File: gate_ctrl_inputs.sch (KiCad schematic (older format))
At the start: 6 parts

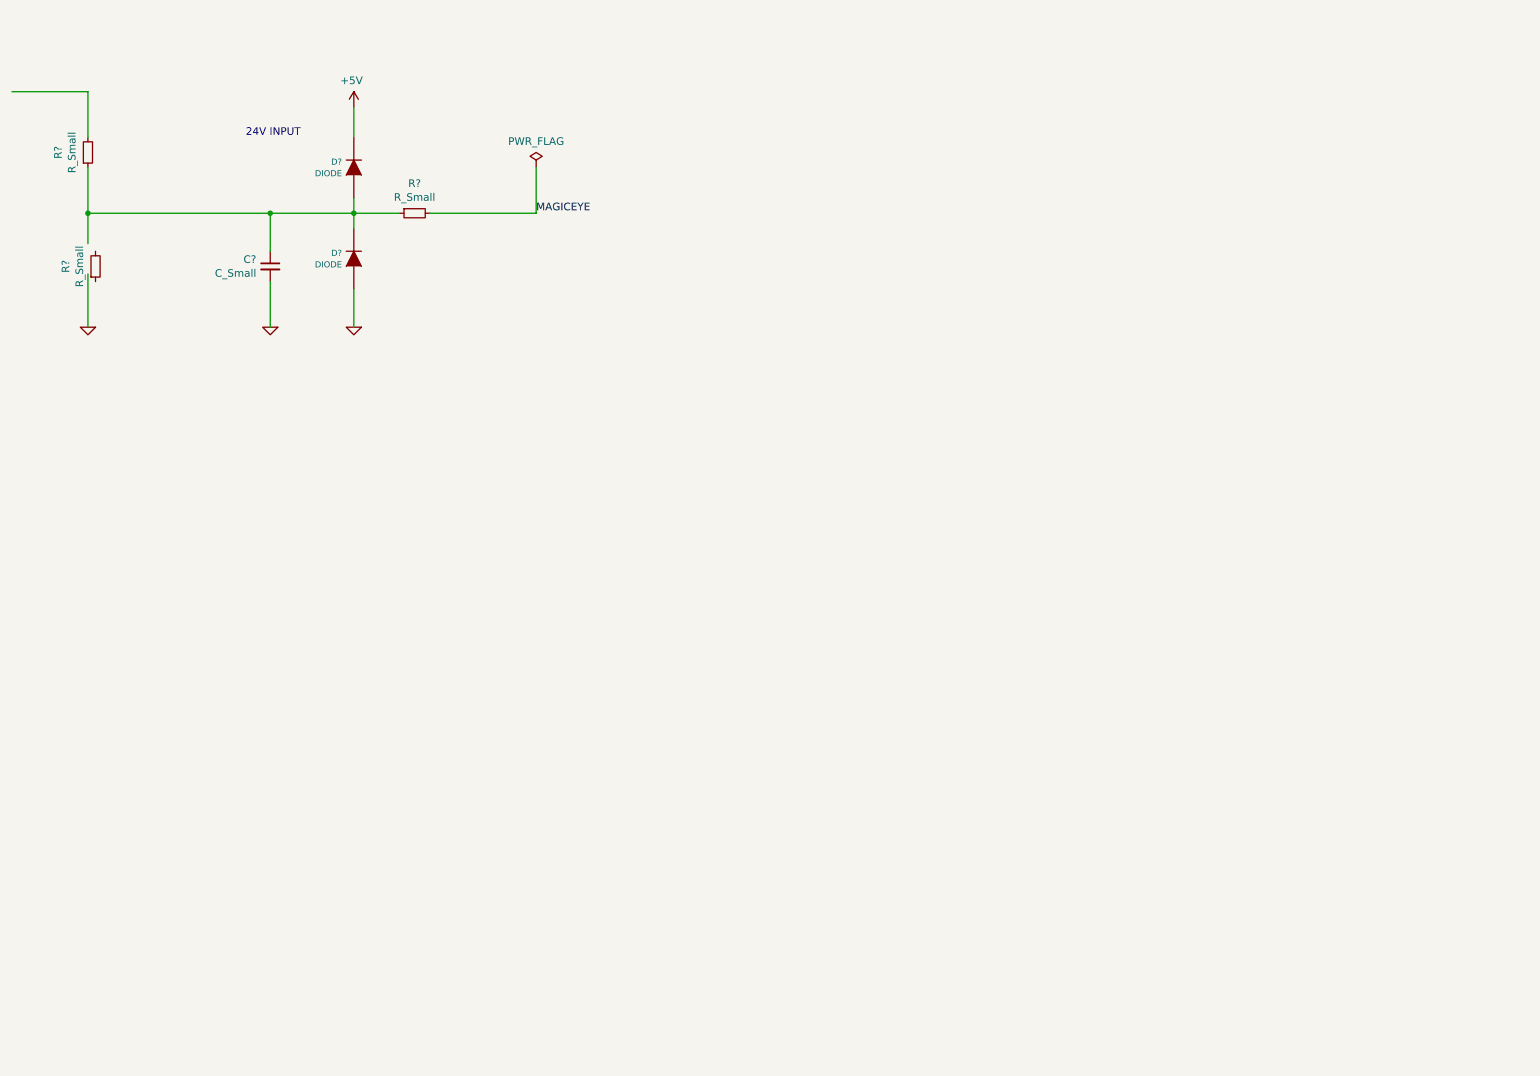
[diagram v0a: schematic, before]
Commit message: Added comments and current sense on 24V supply
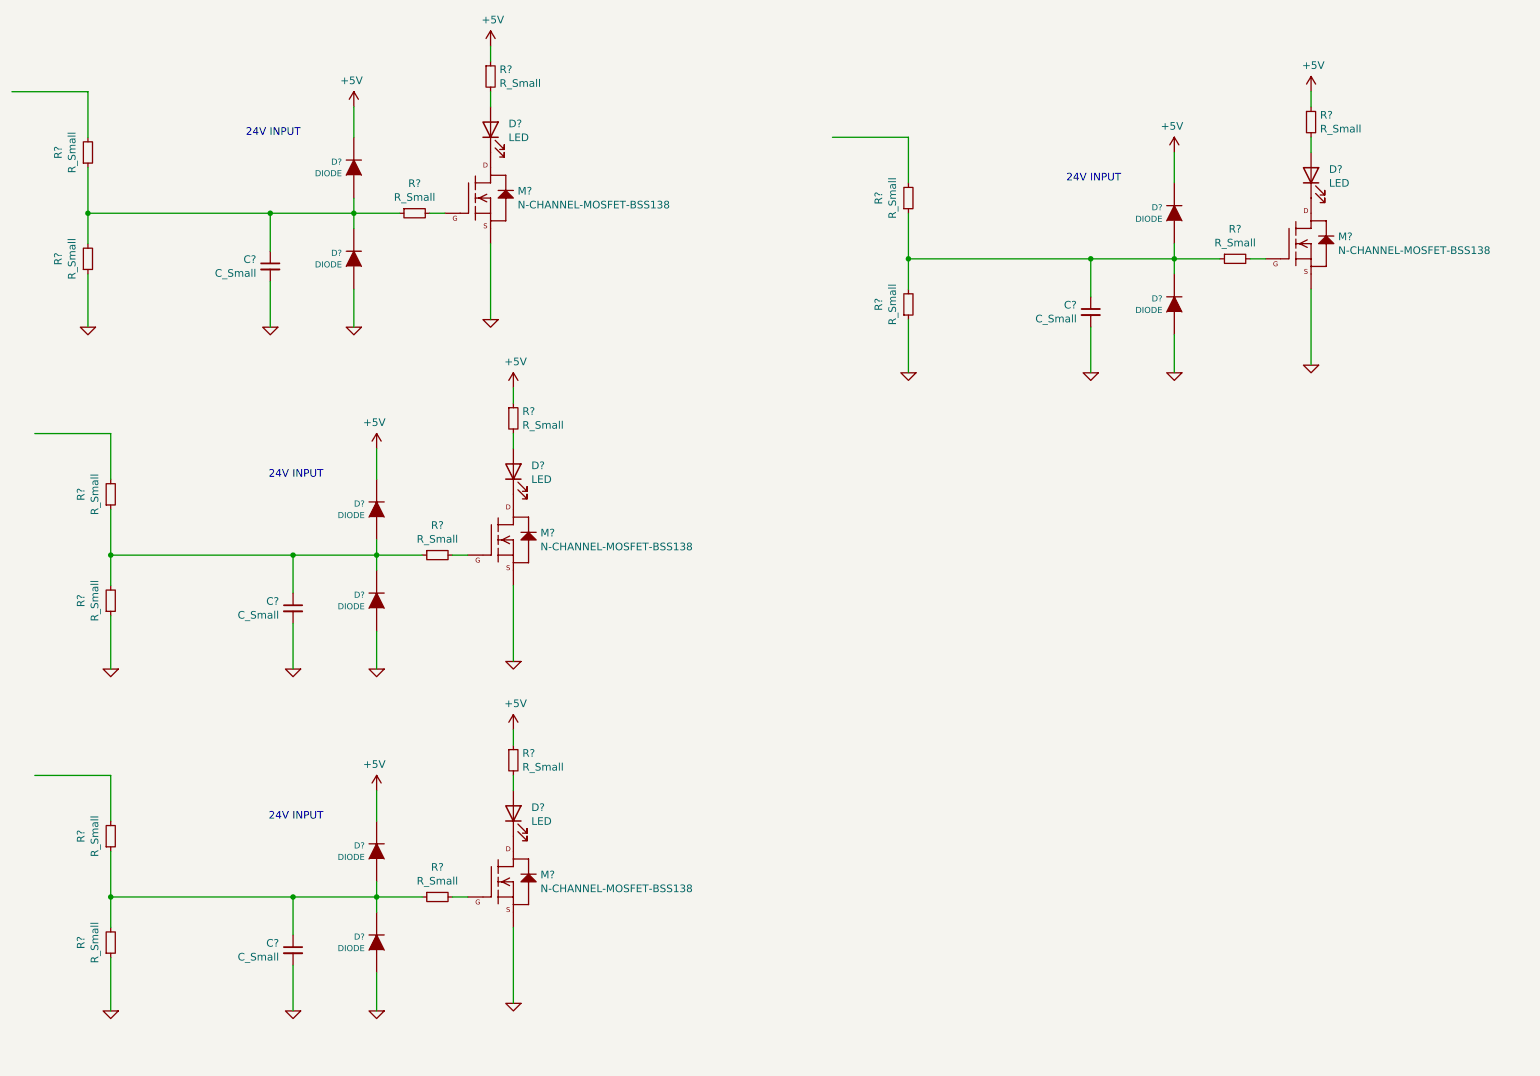
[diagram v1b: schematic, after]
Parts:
- added C? (x3): C_Small, symbol Device:C_Small
- added D? (x4): LED, symbol Device:LED
- added D? (x6): DIODE, symbol GateController-rescue:DIODE-Microtan_65_CPU-cache-AM2
- added M? (x4): N-CHANNEL-MOSFET-BSS138, SOT23-3, symbol GeekAmmo:N-CHANNEL-MOSFET-BSS138
- added R? (x13): R_Small, symbol Device:R_Small
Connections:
- net labels removed: MAGICEYE
- wire segments 16 -> 72
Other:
- moved on the sheet: R?

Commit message: Altered inputs to use bipolar transistors so current is needed to keep them on. This should be more resistant to spikes than Fets, and firmware can filter spikes out. Essentially the inputs are 'harder' to drive.
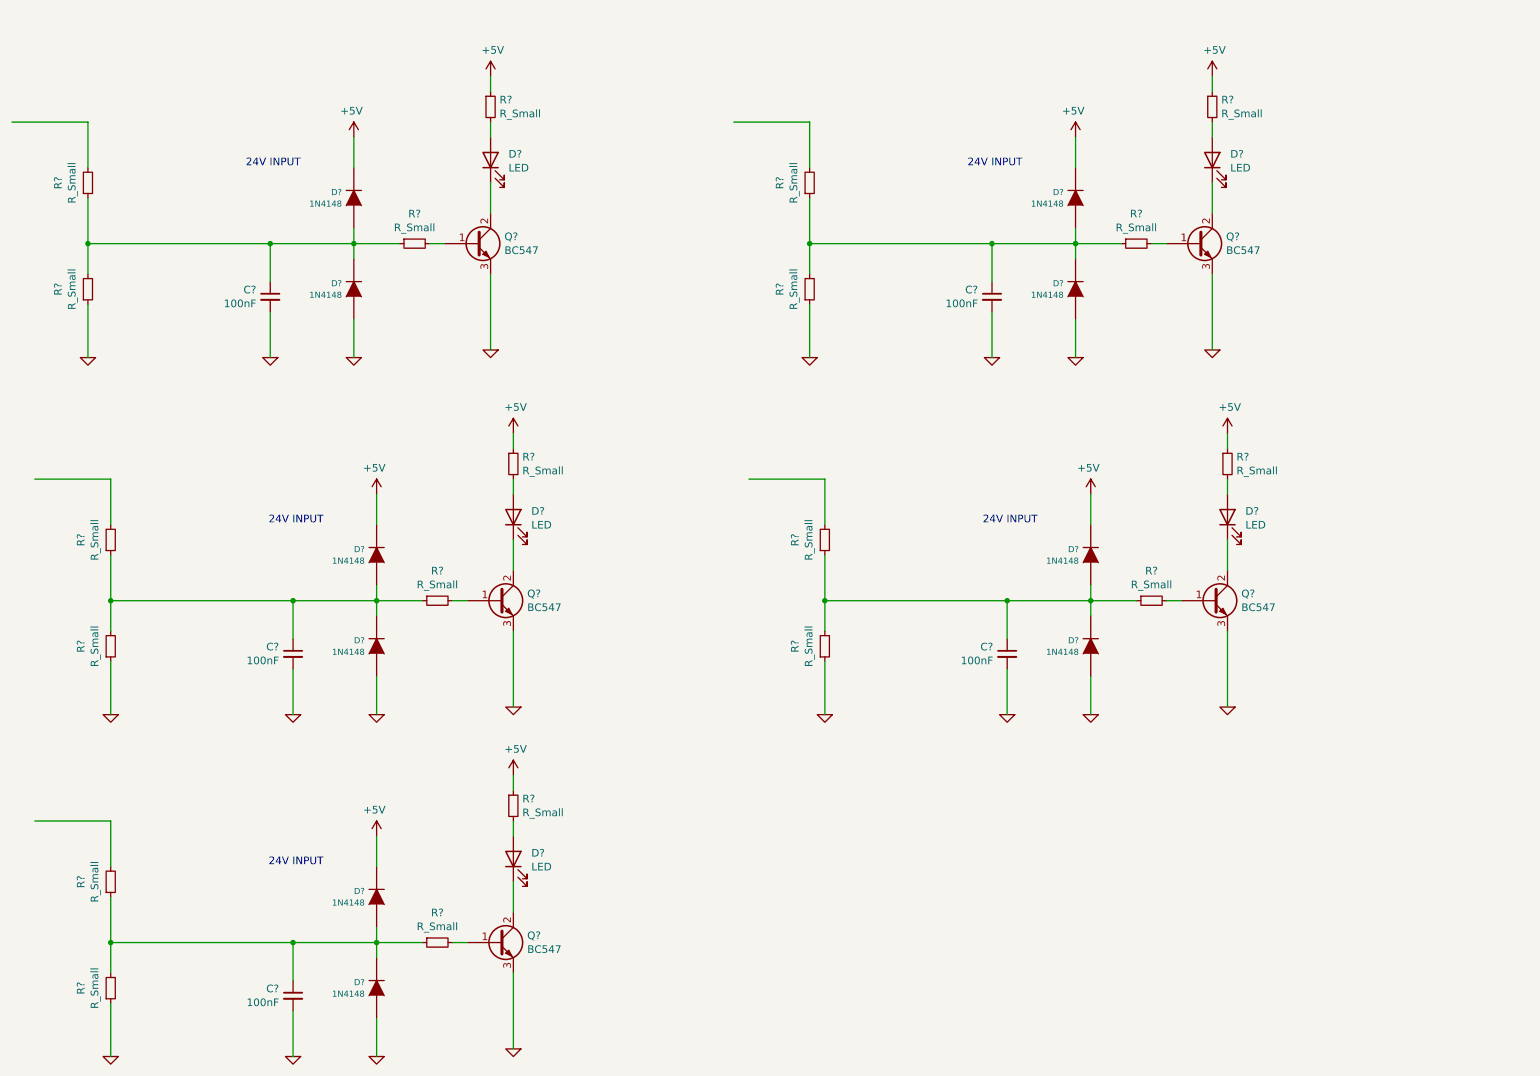
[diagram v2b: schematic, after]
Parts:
- removed C? (x3): C_Small, symbol Device:C_Small
- removed D? (x6): DIODE, symbol GateController-rescue:DIODE-Microtan_65_CPU-cache-AM2
- removed D? (x3): LED, symbol Device:LED
- removed M? (x4): N-CHANNEL-MOSFET-BSS138, SOT23-3, symbol GeekAmmo:N-CHANNEL-MOSFET-BSS138
- removed R? (x12): R_Small, symbol Device:R_Small
- added C? (x4): 100nF, symbol Device:C_Small
- added D? (x8): 1N4148, symbol GateController-rescue:DIODE-Microtan_65_CPU-cache-AM2
- added D? (x4): LED, symbol Device:LED
- added Q? (x5): BC547, symbol Device:Q_NPN_BCE
- added R? (x16): R_Small, symbol Device:R_Small
- C?: value C_Small -> 100nF
- D? (x2): value DIODE -> 1N4148
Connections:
- wire segments 72 -> 95
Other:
- moved on the sheet: C?, D?, R?
